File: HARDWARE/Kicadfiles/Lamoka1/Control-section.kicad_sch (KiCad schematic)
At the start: 53 parts, among them IC1 INA240A2DR, U1 RP2354A, U10 ADS7128IRTER, U2 AMS1117-3.3, U7 TPS62160DSGR, U8 TMP235A2DBZR, X1 ABM8-272-T3

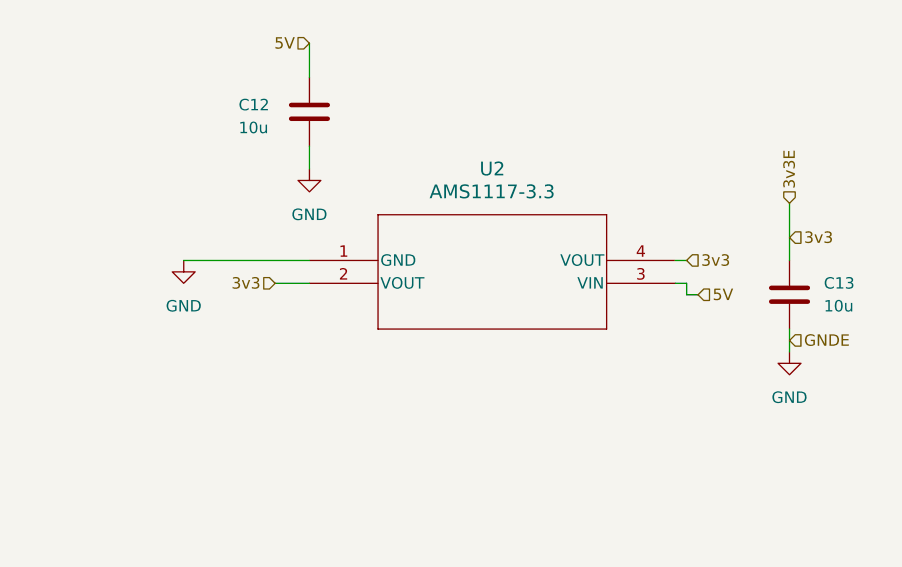
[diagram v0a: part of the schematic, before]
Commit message: ADD H bridge section, tighten everything in PCB routing to be neater. ADD mounting holes M3, etc
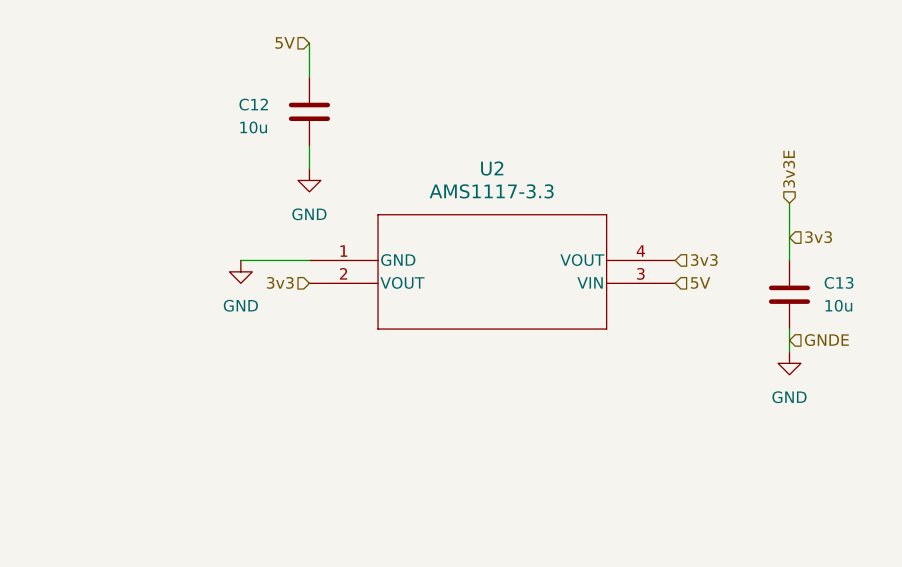
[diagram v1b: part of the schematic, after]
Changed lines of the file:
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@@
 	(wire
 		(pts
-			(xy 67.31 143.51) (xy 81.28 143.51)
+			(xy 73.66 143.51) (xy 81.28 143.51)
 		)
 		(stroke
@@
 	(wire
 		(pts
-			(xy 77.47 146.05) (xy 81.28 146.05)
-		)
-		(stroke
-			(width 0)
-			(type default)
-		)
-	)
-	(wire
-		(pts
 			(xy 87.63 212.09) (xy 87.63 214.63)
 		)
@@
 	(wire
 		(pts
-			(xy 123.19 147.32) (xy 123.19 146.05)
-		)
-		(stroke
-			(width 0)
-			(type default)
-		)
-	)
-	(wire
-		(pts
 			(xy 115.57 204.47) (xy 115.57 203.2)
 		)
@@
 	(wire
 		(pts
-			(xy 123.19 146.05) (xy 121.92 146.05)
-		)
-		(stroke
-			(width 0)
-			(type default)
-		)
-	)
-	(wire
-		(pts
 			(xy 106.68 64.77) (xy 115.57 64.77)
 		)
@@
 	(wire
 		(pts
-			(xy 123.19 147.32) (xy 124.46 147.32)
-		)
-		(stroke
-			(width 0)
-			(type default)
-		)
-	)
-	(wire
-		(pts
 			(xy 134.62 198.12) (xy 139.7 198.12)
 		)
@@
 	(wire
 		(pts
-			(xy 123.19 143.51) (xy 121.92 143.51)
-		)
-		(stroke
-			(width 0)
-			(type default)
-		)
-	)
-	(wire
-		(pts
 			(xy 138.43 200.66) (xy 138.43 198.12)
 		)
@@
 	(hierarchical_label "3v3"
 		(shape input)
-		(at 77.47 146.05 180)
+		(at 81.28 146.05 180)
 		(effects
 			(font
@@
 	(hierarchical_label "3v3"
 		(shape input)
-		(at 123.19 143.51 0)
+		(at 121.92 143.51 0)
 		(effects
 			(font
@@
 	(hierarchical_label "5V"
 		(shape input)
-		(at 124.46 147.32 0)
+		(at 121.92 146.05 0)
 		(effects
 			(font
@@
 	(symbol
 		(lib_id "power:GND")
-		(at 67.31 143.51 0)
+		(at 73.66 143.51 0)
 		(unit 1)
 		(body_style 1)
@@
 		(fields_autoplaced yes)
 		(property "Reference" "#PWR06"
-			(at 67.31 149.86 0)
+			(at 73.66 149.86 0)
 			(hide yes)
 			(show_name no)
@@
 		)
 		(property "Value" "GND"
-			(at 67.31 148.59 0)
+			(at 73.66 148.59 0)
 			(show_name no)
 			(do_not_autoplace no)
@@
 		)
 		(property "Footprint" ""
-			(at 67.31 143.51 0)
+			(at 73.66 143.51 0)
 			(hide yes)
 			(show_name no)
@@
 		)
 		(property "Datasheet" ""
-			(at 67.31 143.51 0)
+			(at 73.66 143.51 0)
 			(hide yes)
 			(show_name no)
@@
 		)
 		(property "Description" "Power symbol creates a global label with name \"GND\" , ground"
-			(at 67.31 143.51 0)
+			(at 73.66 143.51 0)
 			(hide yes)
 			(show_name no)

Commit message: More various routing, finish assigning of all components in inversion and control section. ADD interactive BOM, clean up documentation
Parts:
- C14, C15, C16: footprint components:CAP_0603_CL10A_1P6XP8_SAM -> Capacitor_SMD:C_0603_1608Metric
- C17, C18, C19: footprint (none) -> Capacitor_SMD:C_0402_1005Metric
- C26: footprint (none) -> Capacitor_SMD:C_0603_1608Metric; MPN (none) -> CL10A105KA8NNNC
- C27, C28, C29, C30: footprint (none) -> Capacitor_SMD:C_0603_1608Metric; MPN (none) -> CL10B473KB8NNNC
- L1: footprint components:AOTAB201610S3R3101T -> AOTA-B201610S3R3-101-T:AOTAB201610S3R3101T
- R11, R7: footprint components:RC0402N_PAN -> Resistor_SMD:R_0402_1005Metric
- R22, R26, R28, R30, R32: footprint (none) -> Resistor_SMD:R_0603_1608Metric; MPN (none) -> RC0603FR-0710KL
- R23, R24: footprint (none) -> Resistor_SMD:R_0603_1608Metric; MPN (none) -> RC0603FR-074K7L
- R25: footprint (none) -> Resistor_SMD:R_0603_1608Metric; MPN (none) -> RC0603FR-0736K5L
- R27: footprint (none) -> Resistor_SMD:R_0603_1608Metric; MPN (none) -> RC0603FR-0743K2L
- R29, R31: footprint (none) -> Resistor_SMD:R_0603_1608Metric; MPN (none) -> RC0603FR-0745K3L
- R8: footprint components:RES_CRCW_0603 -> Resistor_SMD:R_0603_1608Metric
- X1: footprint components:ABM8-272-T3_ABR -> ABM8-272-T3:ABM8272T3
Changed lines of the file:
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@@
 			)
 		)
-		(property "Footprint" ""
+		(property "Footprint" "Resistor_SMD:R_0603_1608Metric"
 			(at 283.972 261.62 90)
 			(hide yes)
@@
 			)
 		)
+		(property "MPN" "RC0603FR-074K7L"
+			(at 285.75 261.62 0)
+			(hide yes)
+			(show_name no)
+			(do_not_autoplace no)
+			(effects
+				(font
+					(size 1.27 1.27)
+				)
+			)
+		)
 		(pin "1"
 		)
@@
 			)
 		)
-		(property "Footprint" ""
+		(property "Footprint" "Resistor_SMD:R_0603_1608Metric"
 			(at 85.852 198.12 90)
 			(hide yes)
@@
 			)
 		)
+		(property "MPN" "RC0603FR-0745K3L"
+			(at 87.63 198.12 0)
+			(hide yes)
+			(show_name no)
+			(do_not_autoplace no)
+			(effects
+				(font
+					(size 1.27 1.27)
+				)
+			)
+		)
 		(pin "1"
 		)
@@
 			)
 		)
-		(property "Footprint" ""
+		(property "Footprint" "Resistor_SMD:R_0603_1608Metric"
 			(at 41.91 260.858 90)
 			(hide yes)
@@
 			)
 		)
+		(property "MPN" "RC0603FR-0710KL"
+			(at 41.91 259.08 90)
+			(hide yes)
+			(show_name no)
+			(do_not_autoplace no)
+			(effects
+				(font
+					(size 1.27 1.27)
+				)
+			)
+		)
 		(pin "2"
 		)
@@
 			)
 		)
-		(property "Footprint" "components:CAP_0603_CL10A_1P6XP8_SAM"
+		(property "Footprint" "Capacitor_SMD:C_0603_1608Metric"
 			(at 162.2552 60.96 0)
 			(hide yes)
@@
 			)
 		)
-		(property "Footprint" "components:RES_CRCW_0603"
+		(property "Footprint" "Resistor_SMD:R_0603_1608Metric"
 			(at 162.56 79.248 90)
 			(hide yes)
@@
 			)
 		)
-		(property "Footprint" "components:RC0402N_PAN"
+		(property "Footprint" "Resistor_SMD:R_0402_1005Metric"
 			(at 158.75 97.028 90)
 			(hide yes)
@@
 			)
 		)
-		(property "Footprint" ""
+		(property "Footprint" "Capacitor_SMD:C_0603_1608Metric"
 			(at 77.1652 210.82 0)
 			(hide yes)
@@
 			)
 		)
+		(property "MPN" "CL10B473KB8NNNC"
+			(at 76.2 207.01 0)
+			(hide yes)
+			(show_name no)
+			(do_not_autoplace no)
+			(effects
+				(font
+					(size 1.27 1.27)
+				)
+			)
+		)
 		(pin "1"
 		)
@@
 			)
 		)
-		(property "Footprint" ""
+		(property "Footprint" "Resistor_SMD:R_0603_1608Metric"
 			(at 57.912 207.01 90)
 			(hide yes)
@@
 			)
 		)
+		(property "MPN" "RC0603FR-0710KL"
+			(at 59.69 207.01 0)
+			(hide yes)
+			(show_name no)
+			(do_not_autoplace no)
+			(effects
+				(font
+					(size 1.27 1.27)
+				)
+			)
+		)
 		(pin "1"
 		)
@@
 			)
 		)
-		(property "Footprint" "components:AOTAB201610S3R3101T"
+		(property "Footprint" "AOTA-B201610S3R3-101-T:AOTAB201610S3R3101T"
 			(at 205.74 46.99 0)
 			(hide yes)
@@
 			)
 		)
-		(property "Footprint" ""
+		(property "Footprint" "Resistor_SMD:R_0603_1608Metric"
 			(at 57.912 196.85 90)
 			(hide yes)
@@
 			)
 		)
+		(property "MPN" "RC0603FR-0743K2L"
+			(at 59.69 196.85 0)
+			(hide yes)
+			(show_name no)
+			(do_not_autoplace no)
+			(effects
+				(font
+					(size 1.27 1.27)
+				)
+			)
+		)
 		(pin "1"
 		)
@@
 			)
 		)
-		(property "Footprint" ""
+		(property "Footprint" "Resistor_SMD:R_0603_1608Metric"
 			(at 113.792 198.12 90)
 			(hide yes)
@@
 			)
 		)
+		(property "MPN" "RC0603FR-0745K3L"
+			(at 115.57 198.12 0)
+			(hide yes)
+			(show_name no)
+			(do_not_autoplace no)
+			(effects
+				(font
+					(size 1.27 1.27)
+				)
+			)
+		)
 		(pin "1"
 		)
@@
 			)
 		)
-		(property "Footprint" "components:ABM8-272-T3_ABR"
+		(property "Footprint" "ABM8-272-T3:ABM8272T3"
 			(at 284.48 69.85 0)
 			(hide yes)
@@
 			)
 		)
-		(property "Footprint" ""
+		(property "Footprint" "Resistor_SMD:R_0603_1608Metric"
 			(at 85.852 208.28 90)
 			(hide yes)
@@
 			)
 		)
+		(property "MPN" "RC0603FR-0710KL"
+			(at 87.63 208.28 0)
+			(hide yes)
+			(show_name no)
+			(do_not_autoplace no)
+			(effects
+				(font
+					(size 1.27 1.27)
+				)
+			)
+		)
 		(pin "1"
 		)
@@
 			)
 		)
-		(property "Footprint" ""
+		(property "Footprint" "Capacitor_SMD:C_0402_1005Metric"
 			(at 181.3052 50.8 0)
 			(hide yes)
@@
 			)
 		)
-		(property "Footprint" ""
+		(property "Footprint" "Capacitor_SMD:C_0603_1608Metric"
 			(at 49.2252 209.55 0)
 			(hide yes)
@@
 			)
 		)
+		(property "MPN" "CL10B473KB8NNNC"
+			(at 48.26 205.74 0)
+			(hide yes)
+			(show_name no)
+			(do_not_autoplace no)
+			(effects
+				(font
+					(size 1.27 1.27)
+				)
+			)
+		)
 		(pin "1"
 		)
@@
 			)
 		)
-		(property "Footprint" ""
+		(property "Footprint" "Capacitor_SMD:C_0402_1005Metric"
 			(at 195.58 42.2148 0)
 			(hide yes)
@@
 			)
 		)
-		(property "Footprint" "components:CAP_0603_CL10A_1P6XP8_SAM"
+		(property "Footprint" "Capacitor_SMD:C_0603_1608Metric"
 			(at 178.7652 40.64 0)
 			(hide yes)
@@
 			)
 		)
-		(property "Footprint" ""
+		(property "Footprint" "Resistor_SMD:R_0603_1608Metric"
 			(at 29.972 196.85 90)
 			(hide yes)
@@
 			)
 		)
+		(property "MPN" "RC0603FR-0736K5L"
+			(at 31.75 196.85 0)
+			(hide yes)
+			(show_name no)
+			(do_not_autoplace no)
+			(effects
+				(font
+					(size 1.27 1.27)
+				)
+			)
+		)
 		(pin "1"
 		)
@@
 			)
 		)
-		(property "Footprint" ""
+		(property "Footprint" "Capacitor_SMD:C_0402_1005Metric"
 			(at 243.5352 48.26 0)
 			(hide yes)
@@
 			)
 		)
-		(property "Footprint" ""
+		(property "Footprint" "Capacitor_SMD:C_0603_1608Metric"
 			(at 173.99 265.1252 0)
 			(hide yes)
@@
 			)
 		)
+		(property "MPN" "CL10A105KA8NNNC"
+			(at 177.8 264.16 90)
+			(hide yes)
+			(show_name no)
+			(do_not_autoplace no)
+			(effects
+				(font
+					(size 1.27 1.27)
+				)
+			)
+		)
 		(pin "1"
 		)
@@
 			)
 		)
-		(property "Footprint" ""
+		(property "Footprint" "Resistor_SMD:R_0603_1608Metric"
 			(at 113.792 208.28 90)
 			(hide yes)
@@
 			)
 		)
+		(property "MPN" "RC0603FR-0710KL"
+			(at 115.57 208.28 0)
+			(hide yes)
+			(show_name no)
+			(do_not_autoplace no)
+			(effects
+				(font
+					(size 1.27 1.27)
+				)
+			)
+		)
 		(pin "1"
 		)
@@
 			)
 		)
-		(property "Footprint" ""
+		(property "Footprint" "Capacitor_SMD:C_0603_1608Metric"
 			(at 105.1052 210.82 0)
 			(hide yes)
@@
 			)
 		)
+		(property "MPN" "CL10B473KB8NNNC"
+			(at 104.14 207.01 0)
+			(hide yes)
+			(show_name no)
+			(do_not_autoplace no)
+			(effects
+				(font
+					(size 1.27 1.27)
+				)
+			)
+		)
 		(pin "1"
 		)
@@
 			)
 		)
-		(property "Footprint" ""
+		(property "Footprint" "Capacitor_SMD:C_0603_1608Metric"
 			(at 21.2852 209.55 0)
 			(hide yes)
@@
 			)
 		)
+		(property "MPN" "CL10B473KB8NNNC"
+			(at 20.32 205.74 0)
+			(hide yes)
+			(show_name no)
+			(do_not_autoplace no)
+			(effects
+				(font
+					(size 1.27 1.27)
+				)
+			)
+		)
 		(pin "1"
 		)
@@
 			)
 		)
-		(property "Footprint" "components:CAP_0603_CL10A_1P6XP8_SAM"
+		(property "Footprint" "Capacitor_SMD:C_0603_1608Metric"
 			(at 227.0252 48.26 0)
 			(hide yes)
@@
 			)
 		)
-		(property "Footprint" ""
+		(property "Footprint" "Resistor_SMD:R_0603_1608Metric"
 			(at 29.972 207.01 90)
 			(hide yes)
@@
 			)
 		)
+		(property "MPN" "RC0603FR-0710KL"
+			(at 31.75 207.01 0)
+			(hide yes)
+			(show_name no)
+			(do_not_autoplace no)
+			(effects
+				(font
+					(size 1.27 1.27)
+				)
+			)
+		)
 		(pin "1"
 		)
@@
 			)
 		)
-		(property "Footprint" "components:RC0402N_PAN"
+		(property "Footprint" "Resistor_SMD:R_0402_1005Metric"
 			(at 296.672 86.36 90)
 			(hide yes)
@@
 			)
 		)
-		(property "Footprint" ""
+		(property "Footprint" "Resistor_SMD:R_0603_1608Metric"
 			(at 267.462 261.62 90)
 			(hide yes)
@@
 			(at 269.24 261.62 0)
 			(hide yes)
+			(show_name no)
+			(do_not_autoplace no)
+			(effects
+				(font
+					(size 1.27 1.27)
+				)
+			)
+		)
+		(property "MPN" "RC0603FR-074K7L"
+			(at 269.24 261.62 0)
+			(hide yes)

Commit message: misc fixes to Lamoka1/2
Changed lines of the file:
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@@
 	(rectangle
 		(start 18.288 68.072)
-		(end 75.692 96.52)
+		(end 73.66 96.52)
 		(stroke
 			(width 0)

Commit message: Get DRC down all the way, other misc improvements
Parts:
- C12, C13, C14, C15, C16, C17, C18, C19, C20, C21, C26, C27, C28, C29, C30, C31, R11, R22, R23, R24, R25, R26, R27, R28, R29, R30, R31, R32, R33, R4, R5, R6, R7, R8: KiLib_Generator (none) -> SMD_2terminal_chip_molded
- C25: footprint (none) -> GRM31CR71A226KE15L:G-31_MUR
- IC1: Arrow Part Number (none) -> INA240A2DR; Arrow Price/Stock (none) -> https://www.arrow.com/en/products/ina240a2dr/texas-instrume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; Height (none) -> 1.75; Manufacturer_Name (none) -> Texas Instruments; Manufacturer_Part_Number (none) -> INA240A2DR; Mouser Part Number (none) -> 595-INA240A2DR; Mouser Price/Stock (none) -> https://www.mouser.co.uk/ProductDetail/Texas-Instruments/IN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
- L3: footprint (none) -> PA4332.222NLT:IND_PA4332.222NLT_PUL
- R19: footprint (none) -> RC0603FR-07180KL:RC0603N_YAG
- R20: footprint (none) -> CRCW0402953KFKED:RC0402N_VIS
- R21: footprint (none) -> CRCW0402100KFKED:RES_CRCW_0402_VIS
- U1: KiLib_Generator (none) -> package/no_lead

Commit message: misc fixes
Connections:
- no-connect marks 27 -> 30

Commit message: major reform on the size of the Lamoka1/2
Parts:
- C31: MPN (none) -> CL10B104KB8NNNC
- L3: value 2.2uH, 4.3A -> 2.2uH; Current (none) -> 4.3A
- R33: MPN (none) -> RC0603FR-0722RL
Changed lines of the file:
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@@
 			)
 		)
+		(property "MPN" "CL10B104KB8NNNC"
+			(at 165.1 212.09 90)
+			(hide yes)
+			(show_name no)
+			(do_not_autoplace no)
+			(effects
+				(font
+					(size 1.27 1.27)
+				)
+			)
+		)
 		(property "Manufacturer" ""
 			(at 165.1 212.09 90)
@@
 			)
 		)
-		(property "Value" "2.2uH, 4.3A"
+		(property "Value" "2.2uH"
 			(at 328.93 129.54 0)
 			(show_name no)
@@
 			)
 		)
+		(property "Current" "4.3A"
+			(at 328.93 129.54 0)
+			(hide yes)
+			(show_name no)
+			(do_not_autoplace no)
+			(effects
+				(font
+					(size 1.27 1.27)
+				)
+			)
+		)
 		(property "MPN" "PA4332.222NLT"
 			(at 321.31 134.62 0)
@@
 			(at 168.91 208.28 0)
 			(hide yes)
+			(show_name no)
+			(do_not_autoplace no)
+			(effects
+				(font
+					(size 1.27 1.27)
+				)
+			)
+		)
+		(property "MPN" "RC0603FR-0722RL"
+			(at 168.91 208.28 0)
+			(hide yes)

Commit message: MOSFET ROUTING, AND SUCH
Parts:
- removed R22: 10k, Resistor_SMD:R_0603_1608Metric, symbol Device:R
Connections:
- net GPIO5: no longer names the net of U1.8 (GPIO5)
- net GPIO6: no longer names the net of U1.9 (GPIO6)
- no-connect marks 30 -> 32
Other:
- note removed: "Pull-up for Fan tach"

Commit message: finishing up routing and all of the lamoka1/2
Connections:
- net 11-14v input renamed CSP
- net 17v renamed G4D
- net SW_A renamed Q3S
- net SW_B renamed G4S
- net VBUS renamed USB-5v
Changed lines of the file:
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@@
 		)
 	)
-	(hierarchical_label "GNDE"
+	(hierarchical_label "GND"
 		(shape input)
 		(at 134.62 152.4 0)
@@
 		)
 	)
-	(hierarchical_label "11-14v input"
+	(hierarchical_label "CSP"
 		(shape input)
 		(at 30.48 190.5 180)
@@
 		)
 	)
-	(hierarchical_label "SW_B"
+	(hierarchical_label "G4S"
 		(shape input)
 		(at 113.03 190.5 180)
@@
 		)
 	)
-	(hierarchical_label "SW_A"
+	(hierarchical_label "Q3S"
 		(shape input)
 		(at 85.09 190.5 180)
@@
 		)
 	)
-	(hierarchical_label "FAN-GND"
+	(hierarchical_label "GND"
 		(shape input)
 		(at 29.21 132.08 180)
@@
 		)
 	)
-	(hierarchical_label "11-14v input"
+	(hierarchical_label "CSP"
 		(shape input)
 		(at 252.73 142.24 90)
@@
 		)
 	)
-	(hierarchical_label "3v3E"
+	(hierarchical_label "3v3"
 		(shape input)
 		(at 134.62 137.16 90)
@@
 		)
 	)
-	(hierarchical_label "17v"
+	(hierarchical_label "G4D"
 		(shape input)
 		(at 57.15 190.5 180)
@@
 		)
 	)
-	(hierarchical_label "SHIELD"
+	(hierarchical_label "GND"
 		(shape input)
 		(at 106.68 68.58 180)
@@
 		)
 	)
-	(hierarchical_label "VBUS"
+	(hierarchical_label "USB-5v"
 		(shape input)
 		(at 106.68 40.64 180)
